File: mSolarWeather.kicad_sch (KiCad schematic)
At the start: 73 parts, among them J1 Solar connector, J10 Micro_SD_Card, J2 JST2PH Batt LiFePo4 3.2v, J3 USB C, J4 I2C ext, J6 LUX_I2C module, J7 BME280_I2C module, J8 WIND, J9 RAIN, Q1 PMOS, Q2 PMOS, SW1 SW_Push_Dual, SW2 SW_Push_Dual, U1 TPS63021, U2 BQ25185, U3 ESP32-S3-WROOM-1-N16R2, U4 Ai-Thinker-Ra-01, U5 DS3231MZ

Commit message: Update mSolarWeather.kicad_sch
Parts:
- removed Q1, Q2: PMOS, symbol Simulation_SPICE:PMOS
- added C15: 1uF, Capacitor_SMD:C_0805_2012Metric_Pad1.18x1.45mm_HandSolder, symbol Device:C
- added Q1, Q2: IRLML6401, Package_TO_SOT_SMD:SOT-23, symbol Transistor_FET:IRLML6401
- added R17: 10k, Resistor_SMD:R_0805_2012Metric_Pad1.20x1.40mm_HandSolder, symbol Device:R
- added SW3: SW_Push_Dual, symbol Switch:SW_Push_Dual
- renumbered C3 to C1, C2 to C10, C10 to C11, C11 to C13, C13 to C14, C14 to C16, C15 to C17, C4 to C2, C5 to C3, C6 to C4, C16 to C5, C1 to C6, D3 to D1, D4 to D2, D5 to D3, D6 to D4, D7 to D5, D10 to D6, D1 to D7, F3 to F2, F2 to F3, J10 to J5, R3 to R1, R8 to R10, R9 to R11, R10 to R12, R11 to R13, R12 to R14, R13 to R15, R14 to R16, R15 to R18, R16 to R19, R20 to R2, R17 to R20, R19 to R21, R18 to R3, R21 to R8, R1 to R9, SW2 to SW1, SW1 to SW2
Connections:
- net +3.3V: now also Q1.2 (S), Q2.2 (S), R17.1
- net GND: now also C15.2, SW3.1, SW3.3
- net cmd_I2C_PWR: now also Q2.1 (G)
- net cmd_SD_PWR: now also Q1.1 (G)
- net at C6.1, F3.1: now also Q2.3 (D)
- net Btn_User: now reaches U3.10 (IO17)
- net Btn_User: now also C15.1, R17.2, SW3.2, SW3.4
- net RST_LORA: now reaches U3.11 (IO18)
- net RST_LORA: now also U4.4 (~{RESET})
- net RST_DS: now reaches U3.23 (IO21)
- net RST_DS: now also U5.4 (~{RST})
- net CS_LORA: now reaches U3.34 (IO41)
- net CS_LORA: now also U4.15 (~{NSS})
- net CS_SD: now reaches U3.35 (IO42)
- net CS_SD: now also J5.2 (DAT3/CD)
- net SPI_CLK: now reaches U4.12 (SCK)
- net SPI_CLK: now also J5.5 (CLK)
- net SPI_SO: now reaches U4.13 (MISO)
- net SPI_SI: now reaches U4.14 (MOSI)
- net SPI_SI: now also J5.3 (CMD), J5.7 (DAT0)
- net at C5.1, F2.1: now also Q1.3 (D)
- no-connect marks 21 -> 20
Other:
- note added: "TODO"
- moved on the sheet: C12, C14, SW1

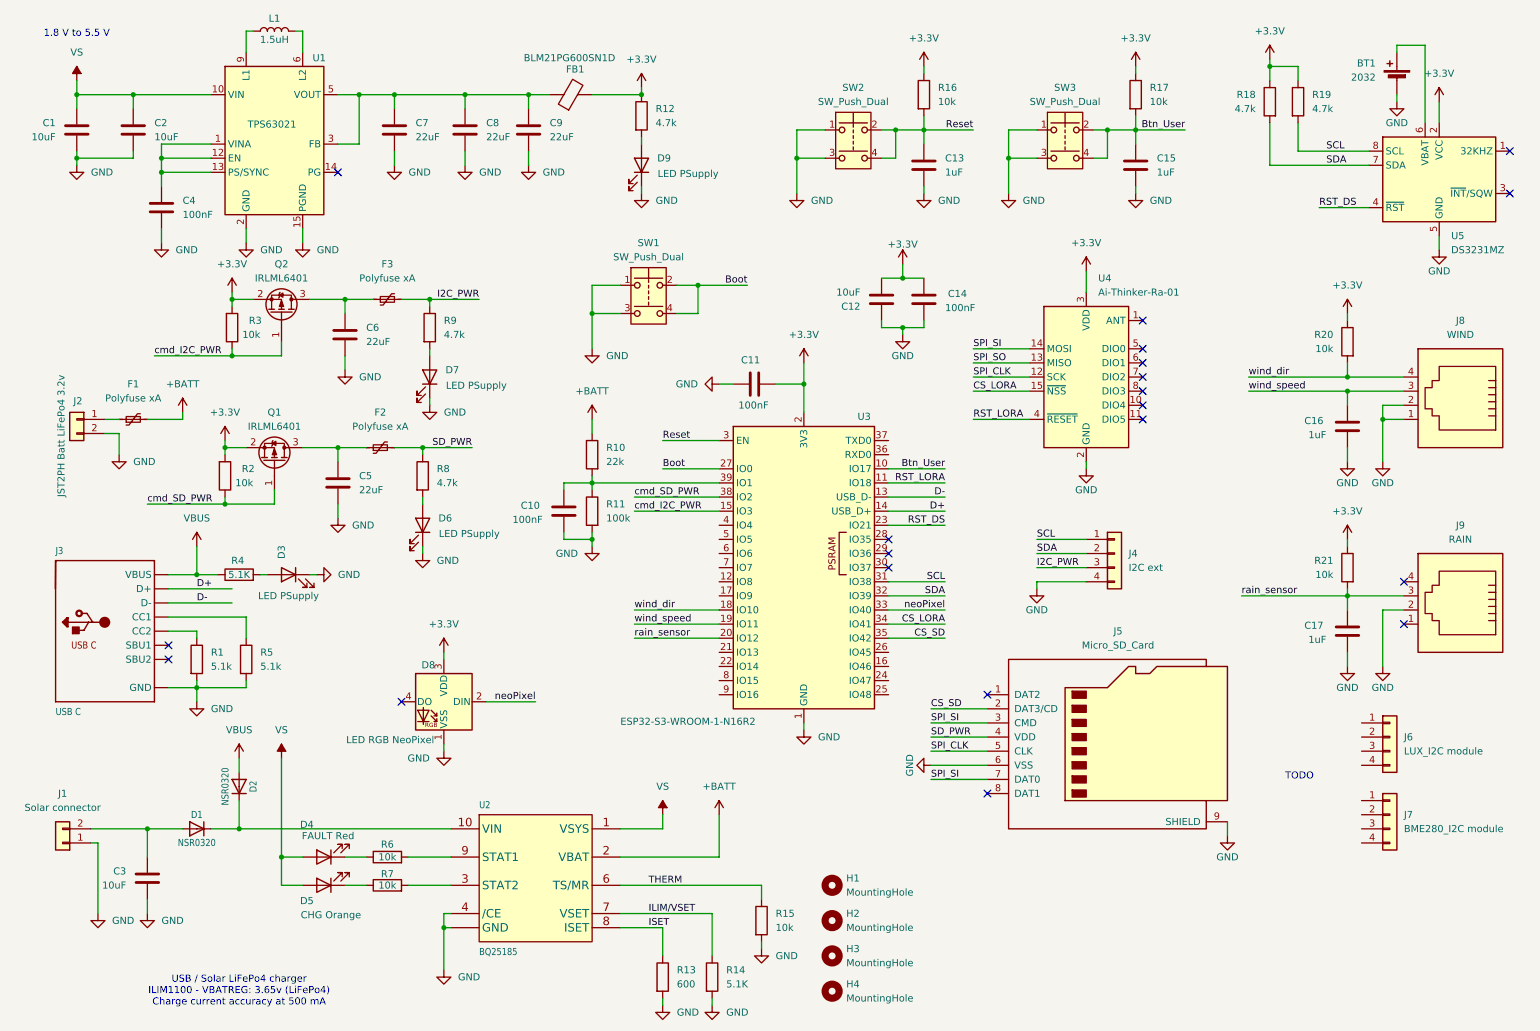
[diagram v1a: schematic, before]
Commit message: Update schema
Update for Kicad 10
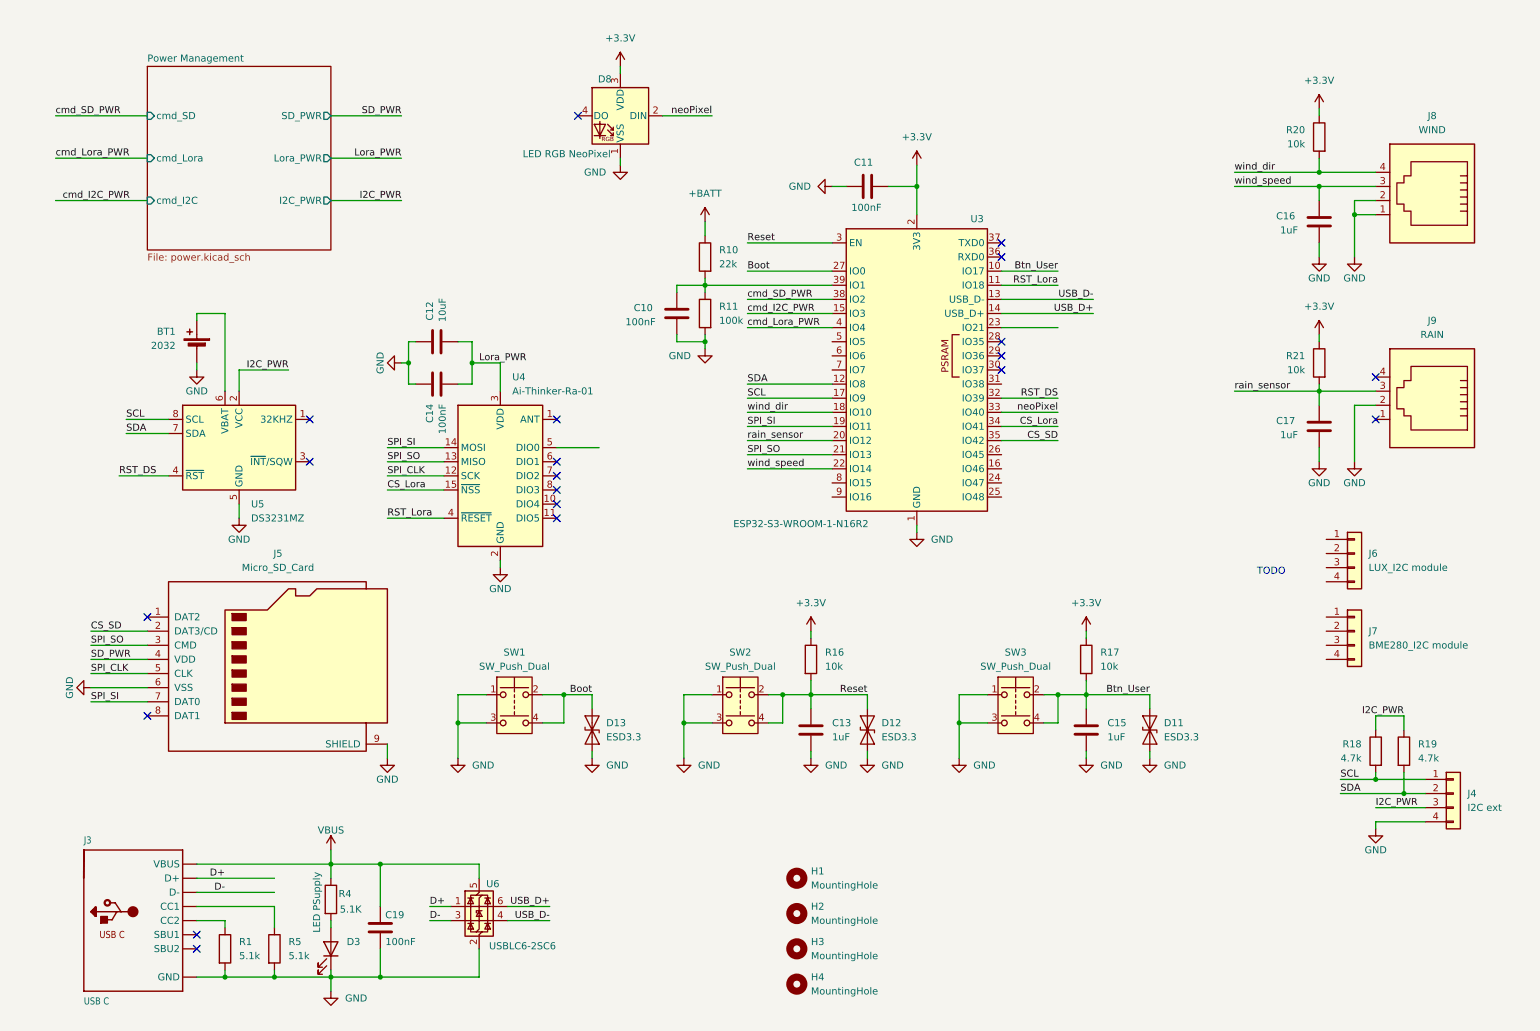
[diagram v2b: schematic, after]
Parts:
- removed C1, C2, C3: 10uF, symbol Device:C
- removed C4: 100nF, Capacitor_SMD:C_0805_2012Metric_Pad1.18x1.45mm_HandSolder, symbol Device:C
- removed C5, C6, C7, C8, C9: 22uF, symbol Device:C
- removed D1, D2: NSR0320, Diode_SMD:D_SOD-323_HandSoldering, symbol lifepo4_solar_charger-eagle-import:DIODE_SOD323MINI
- removed D4: FAULT Red, LED_SMD:LED_PLCC-2_3.4x3.0mm_KA, symbol Device:LED
- removed D5: CHG Orange, LED_SMD:LED_PLCC-2_3.4x3.0mm_KA, symbol Device:LED
- removed D6, D7, D9: LED PSupply, LED_SMD:LED_PLCC-2_3.4x3.0mm_KA, symbol Device:LED
- removed F1, F2, F3: Polyfuse xA, symbol Device:Polyfuse_Small
- removed FB1: BLM21PG600SN1D, Inductor_SMD:L_0805_2012Metric_Pad1.15x1.40mm_HandSolder, symbol Device:FerriteBead
- removed J1: Solar connector, TerminalBlock_Phoenix:TerminalBlock_Phoenix_MKDS-1,5-2-5.08_1x02_P5.08mm_Horizontal, symbol Connector_Generic:Conn_01x02
- removed J2: JST2PH Batt LiFePo4 3.2v, Connector_JST:JST_PH_S2B-PH-K_1x02_P2.00mm_Horizontal, symbol Connector_Generic:Conn_01x02
- removed L1: 1.5uH, Inductor_SMD_Wurth:L_Wurth_WE-LQSH-2010, symbol Device:L
- removed Q1, Q2: IRLML6401, Package_TO_SOT_SMD:SOT-23, symbol Transistor_FET:IRLML6401
- removed R12, R8, R9: 4.7k, Resistor_SMD:R_0805_2012Metric_Pad1.20x1.40mm_HandSolder, symbol Device:R
- removed R13: 600, Resistor_SMD:R_0805_2012Metric_Pad1.20x1.40mm_HandSolder, symbol Device:R
- removed R14: 5.1K, Resistor_SMD:R_0805_2012Metric_Pad1.20x1.40mm_HandSolder, symbol Device:R
- removed R15, R2, R3, R6, R7: 10k, Resistor_SMD:R_0805_2012Metric_Pad1.20x1.40mm_HandSolder, symbol Device:R
- removed U1: TPS63021, mSolarLib:VSON_DSJ-14-3x4mm_P0.5mm_ThermalVias, symbol mSolarLib:TPS63021
- removed U2: BQ25185, Package_SON:WSON-10-1EP_2.5x2.5mm_P0.5mm_EP1.2x2mm_ThermalVias, symbol lifepo4_solar_charger-eagle-import:BQ25185
- added C19: 100nF, Capacitor_SMD:C_0805_2012Metric_Pad1.18x1.45mm_HandSolder, symbol Device:C
- added D11, D12, D13: ESD3.3, Diode_SMD:D_SOD-923, symbol Diode:ESD9B3.3ST5G
- added U6: USBLC6-2SC6, Package_TO_SOT_SMD:SOT-23-6, symbol Power_Protection:USBLC6-2SC6
- J5: footprint (none) -> Connector_Card:microSD_HC_Hirose_DM3AT-SF-PEJM5; Fournisseur (none) -> https://www.mouser.fr/fr/ProductDetail/Hirose-Connector/DM3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
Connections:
- net +3.3V: no longer C12.2, C14.2, R18.1, R19.1, U4.3 (VDD), U5.2 (VCC)
- net Boot: now also D13.2 (A2)
- net Btn_User: now also D11.2 (A2)
- net D+: now also U6.1 (I/O1); no longer U3.14 (USB_D+)
- net D-: now also U6.3 (I/O2); no longer U3.13 (USB_D-)
- net GND: now also C19.1, D11.1 (A1), D12.1 (A1), D13.1 (A1), U6.2 (GND)
- net I2C_PWR: now also R18.1, R19.1, U5.2 (VCC)
- net RST_DS: now also U3.32 (IO39); no longer U3.23 (IO21)
- net Reset: now also D12.2 (A2)
- net SCL: now also R18.2, U3.17 (IO9); no longer R19.2, U3.31 (IO38)
- net SDA: now also R19.2, U3.12 (IO8); no longer R18.2, U3.32 (IO39)
- net SPI_SI: now also U3.19 (IO11); no longer J5.3 (CMD)
- net SPI_SO: now also J5.3 (CMD), U3.21 (IO13)
- net VBUS: now also C19.2, U6.5 (VBUS)
- net wind_speed: now also U3.22 (IO14); no longer U3.19 (IO11)
- net cmd_Lora_PWR: now reaches U3.4 (IO4)
- net CS_LORA renamed CS_Lora
- net RST_LORA renamed RST_Lora
- new net Lora_PWR: C12.2, C14.2, U4.3 (VDD)
- new net USB_D+: U3.14 (USB_D+), U6.6 (I/O1)
- new net USB_D-: U3.13 (USB_D-), U6.4 (I/O2)
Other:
- added sheet Power Management (power.kicad_sch)
- note removed: "1.8 V to 5.5 V"
- note removed: "USB / Solar LiFePo4 charger ILIM1100 - VBATREG: 3.65v (LiFePo4) Charge current accuracy at 500 mA"
- moved on the sheet: H1, H2, H3, H4

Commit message: update footprints
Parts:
- C2: renamed from C12; footprint (none) -> Capacitor_SMD:C_1206_3216Metric_Pad1.33x1.80mm_HandSolder
- renumbered C19 to C1, C14 to C3, C10 to C4, C13 to C5, C11 to C6, C15 to C7, C16 to C8, C17 to C9, D3 to D1, D13 to D2, D8 to D3, D12 to D4, D11 to D5, J3 to J1, J5 to J2, J6 to J3, J7 to J4, J8 to J5, J9 to J6, J4 to J7, R18 to R10, R19 to R11, R5 to R2, R4 to R3, R10 to R4, R11 to R5, R16 to R6, R17 to R7, R20 to R8, R21 to R9, U5 to U1, U6 to U2, U4 to U3, U3 to U4

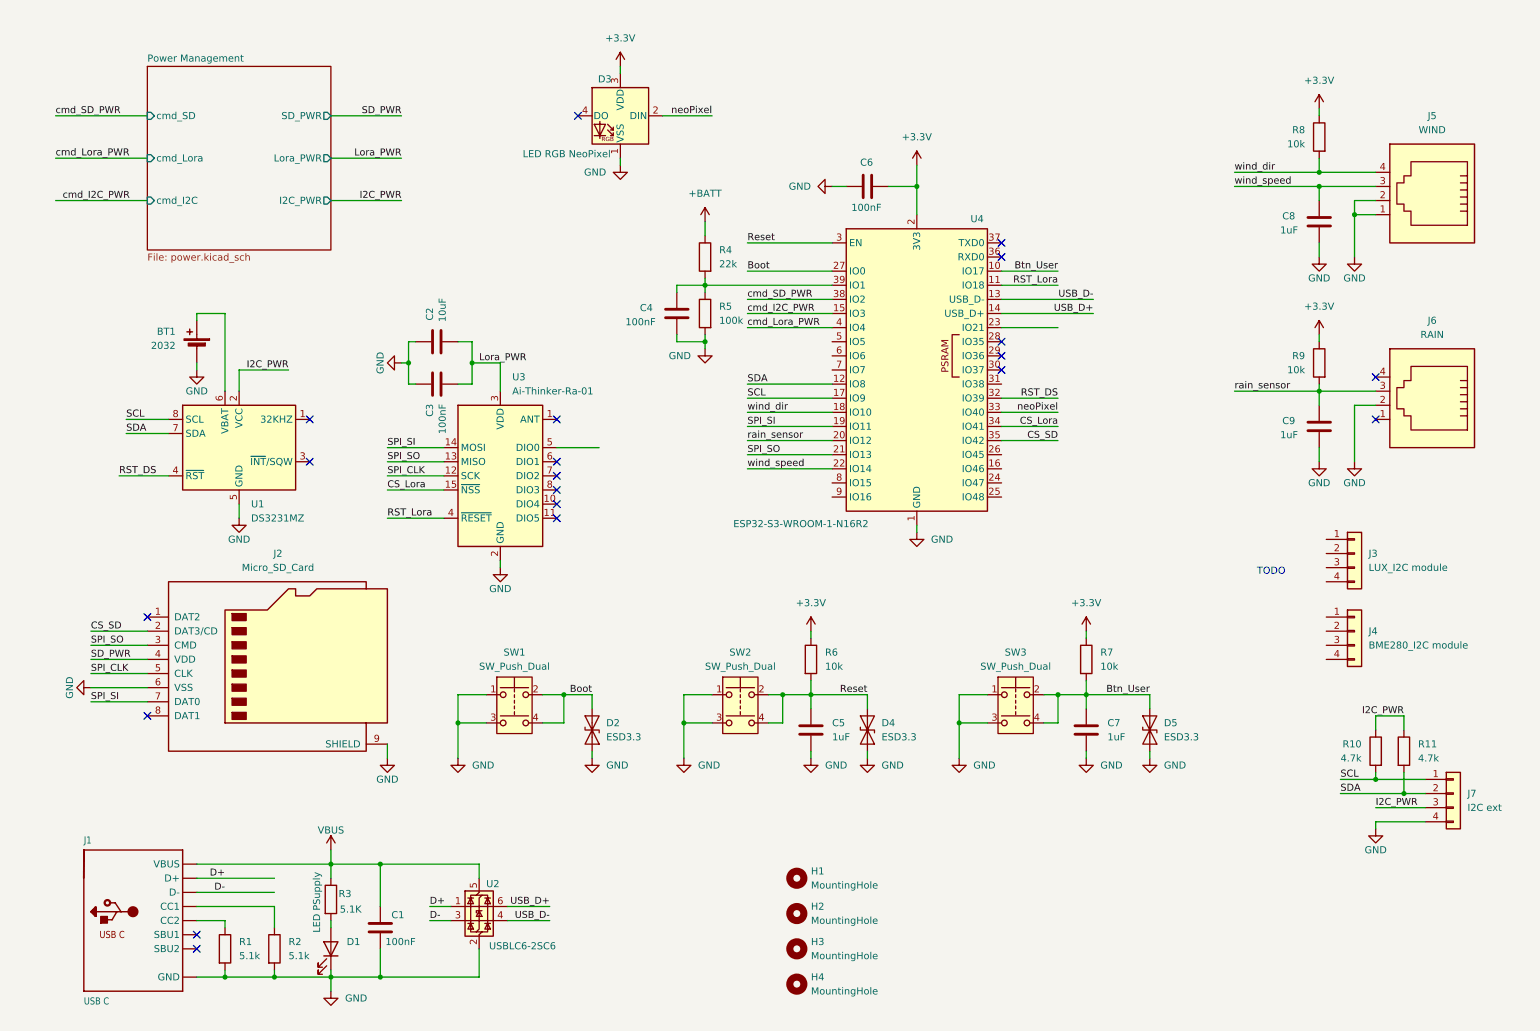
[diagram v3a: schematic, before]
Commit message: update schema
set the correct ESP32 pins
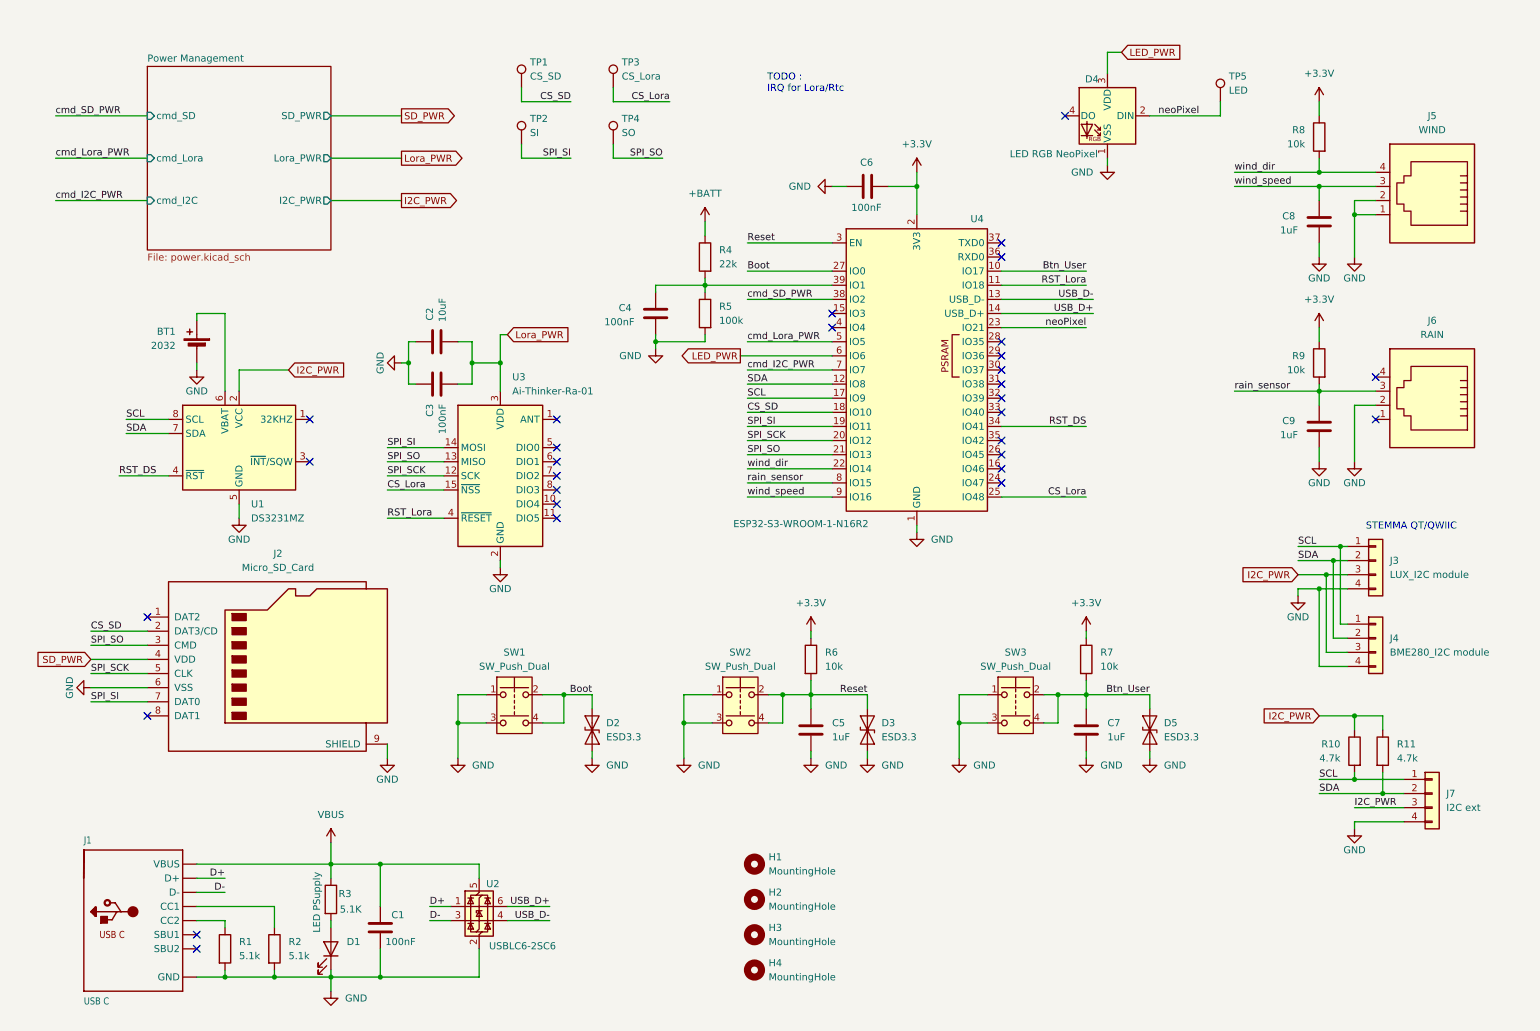
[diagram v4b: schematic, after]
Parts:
- added TP1: CS_SD, TestPoint:TestPoint_Pad_D2.0mm, symbol Connector:TestPoint
- added TP2: SI, TestPoint:TestPoint_Pad_D2.0mm, symbol Connector:TestPoint
- added TP3: CS_Lora, TestPoint:TestPoint_Pad_D2.0mm, symbol Connector:TestPoint
- added TP4: SO, TestPoint:TestPoint_Pad_D2.0mm, symbol Connector:TestPoint
- added TP5: LED, TestPoint:TestPoint_Pad_D2.0mm, symbol Connector:TestPoint
- renumbered D4 to D3, D3 to D4
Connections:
- net +3.3V: no longer D4.3 (VDD)
- net CS_Lora: now also U4.25 (IO48), TP3.1; no longer U4.34 (IO41)
- net CS_SD: now also U4.18 (IO10), TP1.1; no longer U4.35 (IO42)
- net GND: now also J3.4 (Pin_4), J4.4 (Pin_4)
- net I2C_PWR: now also J3.3 (Pin_3), J4.3 (Pin_3)
- net RST_DS: now also U4.34 (IO41); no longer U4.32 (IO39)
- net SCL: now also J3.1 (Pin_1), J4.1 (Pin_1)
- net SDA: now also J3.2 (Pin_2), J4.2 (Pin_2)
- net SPI_SI: now also TP2.1
- net SPI_SO: now also TP4.1
- net cmd_I2C_PWR: now also U4.7 (IO7); no longer U4.15 (IO3)
- net cmd_Lora_PWR: now also U4.5 (IO5); no longer U4.4 (IO4)
- net neoPixel: now also U4.23 (IO21), TP5.1; no longer U4.33 (IO40)
- net rain_sensor: now also U4.8 (IO15); no longer U4.20 (IO12)
- net wind_dir: now also U4.22 (IO14); no longer U4.18 (IO10)
- net wind_speed: now also U4.9 (IO16); no longer U4.22 (IO14)
- net LED_PWR: now reaches U4.6 (IO6)
- net LED_PWR: now also D4.3 (VDD)
- net SPI_CLK renamed SPI_SCK
- net SPI_SCK: now also U4.20 (IO12)
- no-connect marks 20 -> 30
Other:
- note added: "STEMMA QT/QWIIC"
- note added: "TODO : IRQ for Lora/Rtc"
- note removed: "TODO"
- moved on the sheet: C4, D4, H1, H2, H3, H4, J3, J4, J7, R10, R11

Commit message: update schematic
finalize
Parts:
- added C6: 22uF, Capacitor_SMD:C_1210_3225Metric_Pad1.33x2.70mm_HandSolder, symbol Device:C
- TP1, TP2, TP3, TP4, TP5: footprint TestPoint:TestPoint_Pad_D2.0mm -> (none)
- renumbered C9 to C10, C6 to C7, C7 to C8, C8 to C9
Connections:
- net +3.3V: now also C6.2
- net GND: now also C6.1
- net IRQ_Lora: now reaches U4.24 (IO47)
- net IRQ_Lora: now also U3.5 (DIO0)
- net IRQ_DS: now reaches U4.35 (IO42)
- net IRQ_DS: now also U1.3 (~{INT}/SQW)
- no-connect marks 30 -> 26
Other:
- note removed: "TODO : IRQ for Lora/Rtc"

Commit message: clean schematic
Check ERC error ok
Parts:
- removed J1: USB C, Connector_USB:USB_C_Receptacle_GCT_USB4105-xx-A_16P_TopMnt_Horizontal, symbol Adafruit ESP32-S3 Reverse TFT Feather-eagle-import:USB_C
- removed TP1: CS_SD, symbol Connector:TestPoint
- removed TP2: SI, symbol Connector:TestPoint
- removed TP3: CS_Lora, symbol Connector:TestPoint
- removed TP4: SO, symbol Connector:TestPoint
- removed TP5: LED, symbol Connector:TestPoint
- added J1: USB_C_USB2.0, Connector_USB:USB_C_Receptacle_Palconn_UTC16-G, symbol mSolarLib:USB_C_Receptacle_USB2.0_14P
- added J3: Debug 1, Connector_PinHeader_2.54mm:PinHeader_1x06_P2.54mm_Vertical, symbol Connector:Conn_01x06_Pin
- added J4: Debug 2, Connector_PinHeader_2.54mm:PinHeader_1x06_P2.54mm_Vertical, symbol Connector:Conn_01x06_Pin
- BT1: value 2032 -> CR1220; footprint Battery:BatteryHolder_MYOUNG_BS-07-A1BJ001_CR2032 -> Battery:BatteryHolder_Keystone_500
- J2: Fournisseur https://www.mouser.fr/fr/ProductDetail/Hirose-Connector/DM3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 -> (none); ref (none) -> https://www.mouser.fr/fr/ProductDetail/Hirose-Connector/DM3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
- SW1, SW2, SW3: footprint (none) -> Button_Switch_SMD:SW_Push_1P1T_NO_CK_KSC9xxG
- U4: Mouser https://www.mouser.fr/ProductDetail/356-ESP32S3WRM1N16R2 -> (none); ref (none) -> https://www.mouser.fr/ProductDetail/356-ESP32S3WRM1N16R2
- renumbered C2 to C1, C3 to C2, C1 to C3, J3 to J5, J4 to J6, J5 to J7, J6 to J8, J7 to J9, U3 to U2, U2 to U3
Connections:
- net CS_Lora: now also J3.5 (Pin_5)
- net CS_SD: now also J3.4 (Pin_4)
- net D+: now also J1.A6 (D+), J1.B6 (D+)
- net D-: now also J1.A7 (D-), J1.B7 (D-)
- net GND: now also J2.SH (SHIELD), J1.A1 (GND), J1.A12 (GND), J1.B1 (GND), J1.B12 (GND), J1.SH (SHIELD), J4.6 (Pin_6); no longer J2.9 (SHIELD)
- net IRQ_DS: now also J4.4 (Pin_4)
- net IRQ_Lora: now also J3.6 (Pin_6)
- net SPI_SCK: now also J3.3 (Pin_3)
- net SPI_SI: now also J3.1 (Pin_1)
- net SPI_SO: now also J3.2 (Pin_2)
- net VBUS: now also J1.A4 (VBUS), J1.A9 (VBUS), J1.B4 (VBUS), J1.B9 (VBUS)
- net neoPixel: now also J4.5 (Pin_5)
- net rain_sensor: now also J4.3 (Pin_3)
- net wind_dir: now also J4.1 (Pin_1)
- net wind_speed: now also J4.2 (Pin_2)
- net at R2.1: now also J1.A5 (CC1)
- net at R1.1: now also J1.B5 (CC2)
- no-connect marks 26 -> 24
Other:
- moved on the sheet: BT1, C3, D1, R1, R2, R3, U1, U3
